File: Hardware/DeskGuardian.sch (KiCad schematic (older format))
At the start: 7 parts

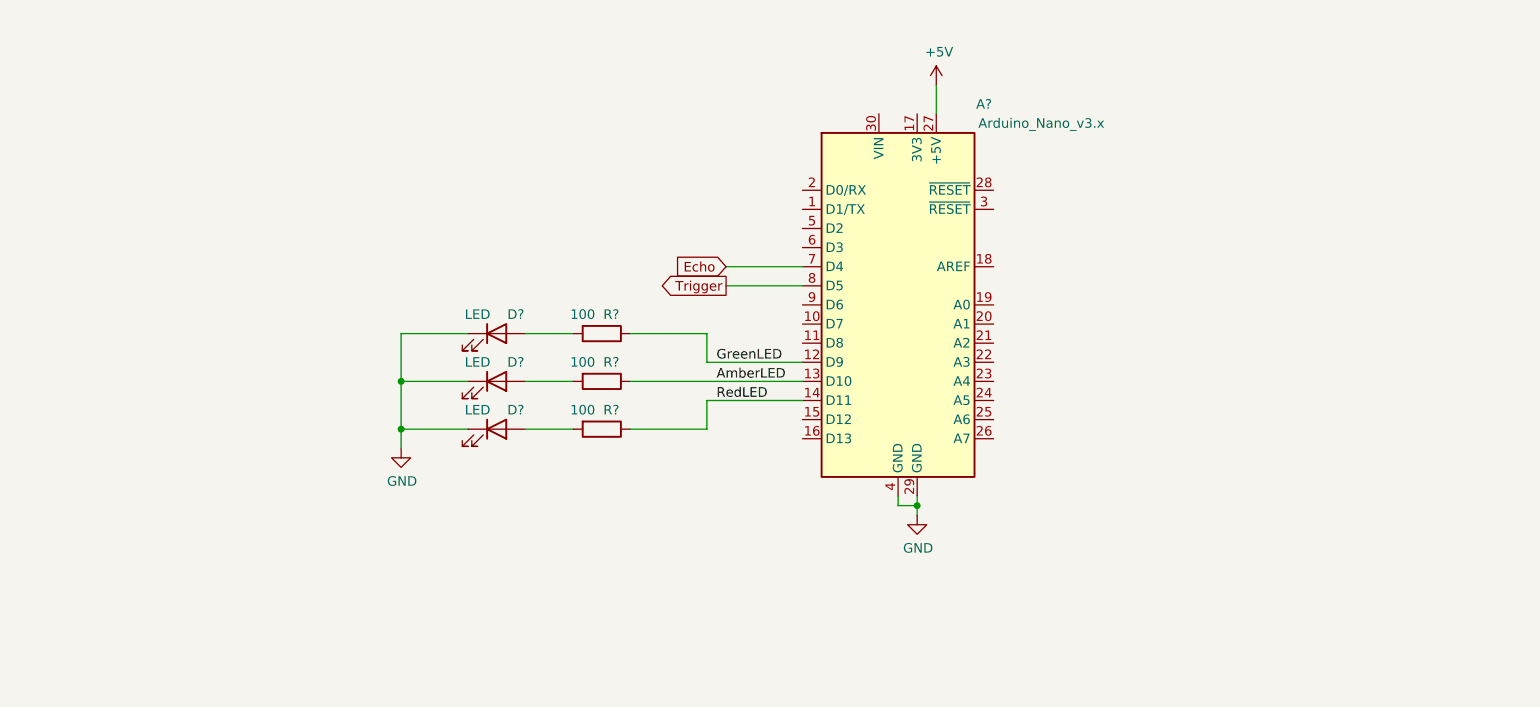
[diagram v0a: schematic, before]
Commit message: Full rework of instructions
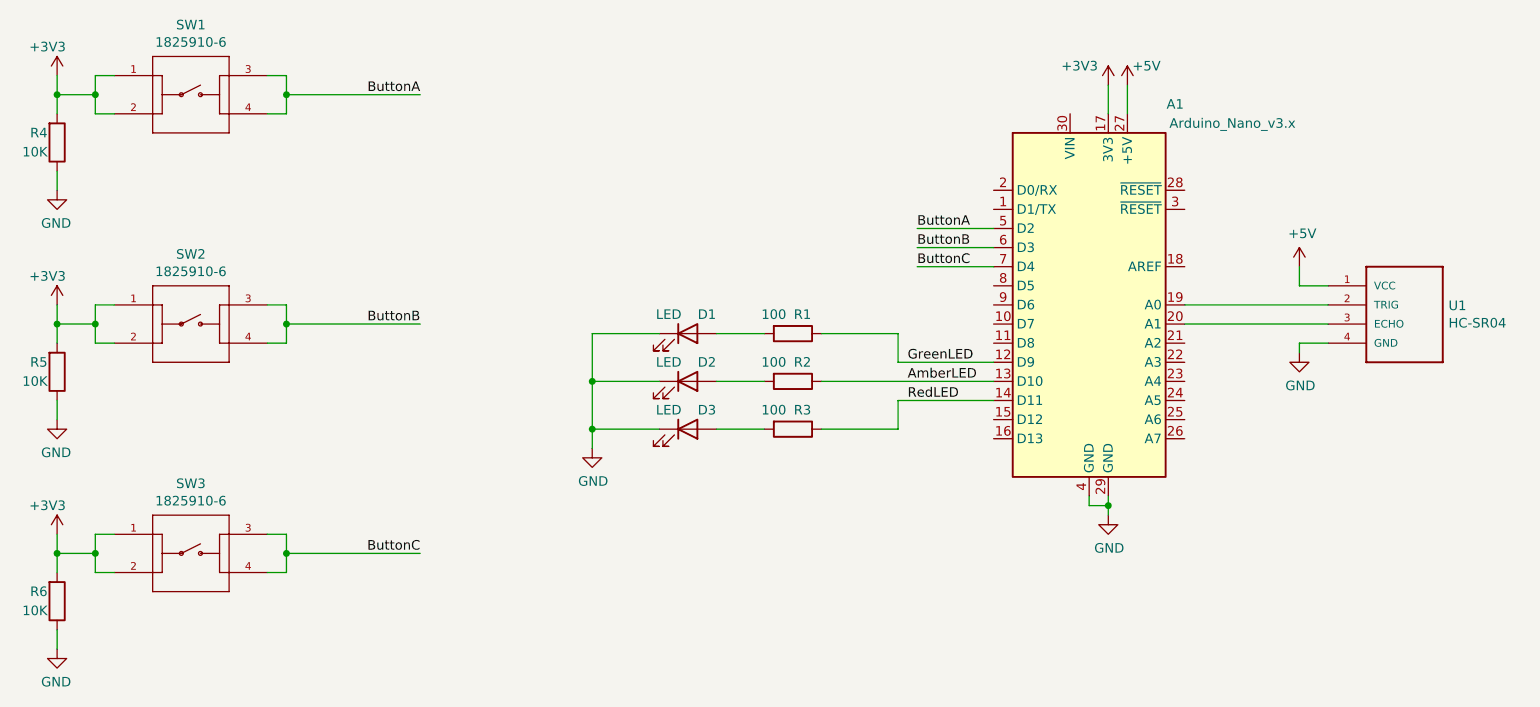
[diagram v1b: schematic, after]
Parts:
- added R4, R5, R6: 10K, symbol Device:R
- added SW1, SW2, SW3: 1825910-6, SW_1825910-6-4, symbol 1825910-6:1825910-6
- added U1: HC-SR04, XCVR_HC-SR04, symbol HC-SR04:HC-SR04
- gave numbers to parts that had none: 7
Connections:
- net +5V: now also U1.1 (VCC)
- net GND: now also R4.1, R5.1, R6.1, U1.4 (GND)
- net +3V3: now reaches A1.17 (3V3)
- net +3V3: now also R4.2, R5.2, R6.2, SW1.1, SW1.2, SW2.1, SW2.2, SW3.1, SW3.2
- net at A1.19 (A0): now also U1.2 (TRIG)
- net at A1.20 (A1): now also U1.3 (ECHO)
- net ButtonA: now reaches A1.5 (D2)
- net ButtonA: now also SW1.3, SW1.4
- net ButtonB: now reaches A1.6 (D3)
- net ButtonB: now also SW2.3, SW2.4
- net Echo renamed ButtonC
- net ButtonC: now also SW3.3, SW3.4
- net Trigger: no longer names the net of A1.8 (D5)
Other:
- moved on the sheet: A1, D1, D2, D3, R1, R2, R3

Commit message: updated schematic
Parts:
- D1, D2, D3: footprint (none) -> LED_THT:LED_D5.0mm
- R1: renamed from R4; footprint (none) -> Resistor_SMD:R_1206_3216Metric_Pad1.42x1.75mm_HandSolder
- R2: renamed from R5; footprint (none) -> Resistor_SMD:R_1206_3216Metric_Pad1.42x1.75mm_HandSolder
- R3: renamed from R6; footprint (none) -> Resistor_SMD:R_1206_3216Metric_Pad1.42x1.75mm_HandSolder
- R4: renamed from R1; footprint (none) -> Resistor_SMD:R_1206_3216Metric_Pad1.42x1.75mm_HandSolder
- R5: renamed from R2; footprint (none) -> Resistor_SMD:R_1206_3216Metric_Pad1.42x1.75mm_HandSolder
- R6: renamed from R3; footprint (none) -> Resistor_SMD:R_1206_3216Metric_Pad1.42x1.75mm_HandSolder
- SW1, SW2, SW3: footprint SW_1825910-6-4 -> Footprints:SW_1825910-6-4
- U1: footprint XCVR_HC-SR04 -> Footprints:XCVR_HC-SR04
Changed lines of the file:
@@
 $EndDescr
 $Comp
-L power:GND #PWR0101
+L power:GND #PWR09
 U 1 1 5F31EFDB
 P 7000 4500
-F 0 "#PWR0101" H 7000 4250 50  0001 C CNN
+F 0 "#PWR09" H 7000 4250 50  0001 C CNN
 F 1 "GND" H 7005 4327 50  0000 C CNN
 F 2 "" H 7000 4500 50  0001 C CNN
@@
 $EndComp
 $Comp
-L Device:R R4
+L Device:R R1
 U 1 1 5F35D6A2
 P 1500 2550
-F 0 "R4" H 1450 2500 50  0000 R CNN
+F 0 "R1" H 1450 2500 50  0000 R CNN
 F 1 "10K" H 1450 2600 50  0000 R CNN
-F 2 "" V 1430 2550 50  0001 C CNN
+F 2 "Resistor_SMD:R_1206_3216Metric_Pad1.42x1.75mm_HandSolder" V 1430 2550 50  0001 C CNN
 F 3 "~" H 1500 2550 50  0001 C CNN
 	1    1500 2550
@@
 	7000 2400 7000 2250
 $Comp
-L power:+5V #PWR0102
+L power:+5V #PWR010
 U 1 1 5F31F7F8
 P 7100 2250
-F 0 "#PWR0102" H 7100 2100 50  0001 C CNN
+F 0 "#PWR010" H 7100 2100 50  0001 C CNN
 F 1 "+5V" H 7200 2350 50  0000 C CNN
 F 2 "" H 7100 2250 50  0001 C CNN
@@
 $EndComp
 $Comp
-L power:+3V3 #PWR05
+L power:+3V3 #PWR08
 U 1 1 5F39EB8C
 P 7000 2250
-F 0 "#PWR05" H 7000 2100 50  0001 C CNN
+F 0 "#PWR08" H 7000 2100 50  0001 C CNN
 F 1 "+3V3" H 6850 2350 50  0000 C CNN
 F 2 "" H 7000 2250 50  0001 C CNN
@@
 	8150 3300 8000 3300
 $Comp
-L power:+5V #PWR06
+L power:+5V #PWR011
 U 1 1 5F3582F6
 P 8000 3200
-F 0 "#PWR06" H 8000 3050 50  0001 C CNN
+F 0 "#PWR011" H 8000 3050 50  0001 C CNN
 F 1 "+5V" H 8015 3373 50  0000 C CNN
 F 2 "" H 8000 3200 50  0001 C CNN
@@
 $EndComp
 $Comp
-L power:GND #PWR07
+L power:GND #PWR012
 U 1 1 5F357FB1
 P 8000 3650
-F 0 "#PWR07" H 8000 3400 50  0001 C CNN
+F 0 "#PWR012" H 8000 3400 50  0001 C CNN
 F 1 "GND" H 8005 3477 50  0000 C CNN
 F 2 "" H 8000 3650 50  0001 C CNN
@@
 F 0 "U1" H 8780 3396 50  0000 L CNN
 F 1 "HC-SR04" H 8780 3305 50  0000 L CNN
-F 2 "XCVR_HC-SR04" H 8350 3400 50  0001 L BNN
+F 2 "Footprints:XCVR_HC-SR04" H 8350 3400 50  0001 L BNN
 F 3 "Osepp" H 8350 3400 50  0001 L BNN
 	1    8350 3400
@@
 	6400 3000 6000 3000
 $Comp
-L Device:R R1
+L Device:R R4
 U 1 1 5F338E4B
 P 5350 3550
-F 0 "R1" V 5250 3600 50  0000 C CNN
+F 0 "R4" V 5250 3600 50  0000 C CNN
 F 1 "100" V 5250 3450 50  0000 C CNN
-F 2 "" V 5280 3550 50  0001 C CNN
+F 2 "Resistor_SMD:R_1206_3216Metric_Pad1.42x1.75mm_HandSolder" V 5280 3550 50  0001 C CNN
 F 3 "~" H 5350 3550 50  0001 C CNN
 	1    5350 3550
@@
 $EndComp
 $Comp
-L Device:R R2
+L Device:R R5
 U 1 1 5F3392D8
 P 5350 3800
-F 0 "R2" V 5250 3850 50  0000 C CNN
+F 0 "R5" V 5250 3850 50  0000 C CNN
 F 1 "100" V 5250 3700 50  0000 C CNN
-F 2 "" V 5280 3800 50  0001 C CNN
+F 2 "Resistor_SMD:R_1206_3216Metric_Pad1.42x1.75mm_HandSolder" V 5280 3800 50  0001 C CNN
 F 3 "~" H 5350 3800 50  0001 C CNN
 	1    5350 3800
@@
 	4650 4050 4300 4050
 $Comp
-L power:GND #PWR0103
+L power:GND #PWR07
 U 1 1 5F33E95F
 P 4300 4150
-F 0 "#PWR0103" H 4300 3900 50  0001 C CNN
+F 0 "#PWR07" H 4300 3900 50  0001 C CNN
 F 1 "GND" H 4305 3977 50  0000 C CNN
 F 2 "" H 4300 4150 50  0001 C CNN
@@
 	5200 3800 4950 3800
 $Comp
-L Device:R R3
+L Device:R R6
 U 1 1 5F3395DB
 P 5350 4050
-F 0 "R3" V 5250 4100 50  0000 C CNN
+F 0 "R6" V 5250 4100 50  0000 C CNN
 F 1 "100" V 5250 3950 50  0000 C CNN
-F 2 "" V 5280 4050 50  0001 C CNN
+F 2 "Resistor_SMD:R_1206_3216Metric_Pad1.42x1.75mm_HandSolder" V 5280 4050 50  0001 C CNN
 F 3 "~" H 5350 4050 50  0001 C CNN
 	1    5350 4050
@@
 F 0 "D3" H 4900 4150 50  0000 C CNN
 F 1 "LED" H 4700 4150 50  0000 C CNN
-F 2 "" H 4800 4050 50  0001 C CNN
+F 2 "LED_THT:LED_D5.0mm" H 4800 4050 50  0001 C CNN
 F 3 "~" H 4800 4050 50  0001 C CNN
 	1    4800 4050
@@
 F 0 "D2" H 4900 3900 50  0000 C CNN
 F 1 "LED" H 4700 3900 50  0000 C CNN
-F 2 "" H 4800 3800 50  0001 C CNN
+F 2 "LED_THT:LED_D5.0mm" H 4800 3800 50  0001 C CNN
 F 3 "~" H 4800 3800 50  0001 C CNN
 	1    4800 3800
@@
 F 0 "D1" H 4900 3650 50  0000 C CNN
 F 1 "LED" H 4700 3650 50  0000 C CNN
-F 2 "" H 4800 3550 50  0001 C CNN
+F 2 "LED_THT:LED_D5.0mm" H 4800 3550 50  0001 C CNN
 F 3 "~" H 4800 3550 50  0001 C CNN
 	1    4800 3550
@@
 F 0 "SW1" H 2200 2665 50  0000 C CNN
 F 1 "1825910-6" H 2200 2574 50  0000 C CNN
-F 2 "SW_1825910-6-4" H 2200 2300 50  0001 L BNN
+F 2 "Footprints:SW_1825910-6-4" H 2200 2300 50  0001 L BNN
 F 3 "Compliant" H 2200 2300 50  0001 L BNN
 F 4 "50 mA" H 2200 2300 50  0001 L BNN "Field4"
@@
 Connection ~ 2700 2300
 $Comp
-L Device:R R5
+L Device:R R2
 U 1 1 5F40E2B9
 P 1500 3750
-F 0 "R5" H 1450 3700 50  0000 R CNN
+F 0 "R2" H 1450 3700 50  0000 R CNN
 F 1 "10K" H 1450 3800 50  0000 R CNN
-F 2 "" V 1430 3750 50  0001 C CNN
+F 2 "Resistor_SMD:R_1206_3216Metric_Pad1.42x1.75mm_HandSolder" V 1430 3750 50  0001 C CNN
 F 3 "~" H 1500 3750 50  0001 C CNN
 	1    1500 3750
@@
 F 0 "SW2" H 2200 3865 50  0000 C CNN
 F 1 "1825910-6" H 2200 3774 50  0000 C CNN
-F 2 "SW_1825910-6-4" H 2200 3500 50  0001 L BNN
+F 2 "Footprints:SW_1825910-6-4" H 2200 3500 50  0001 L BNN
 F 3 "Compliant" H 2200 3500 50  0001 L BNN
 F 4 "50 mA" H 2200 3500 50  0001 L BNN "Field4"
@@
 Connection ~ 2700 3500
 $Comp
-L Device:R R6
+L Device:R R3
 U 1 1 5F41D33F
 P 1500 4950
-F 0 "R6" H 1450 4900 50  0000 R CNN
+F 0 "R3" H 1450 4900 50  0000 R CNN
 F 1 "10K" H 1450 5000 50  0000 R CNN
-F 2 "" V 1430 4950 50  0001 C CNN
+F 2 "Resistor_SMD:R_1206_3216Metric_Pad1.42x1.75mm_HandSolder" V 1430 4950 50  0001 C CNN
 F 3 "~" H 1500 4950 50  0001 C CNN
 	1    1500 4950
@@
 $EndComp
 $Comp
-L power:GND #PWR09
+L power:GND #PWR06
 U 1 1 5F41D345
 P 1500 5200
-F 0 "#PWR09" H 1500 4950 50  0001 C CNN
+F 0 "#PWR06" H 1500 4950 50  0001 C CNN
 F 1 "GND" H 1505 5027 50  0000 C CNN
 F 2 "" H 1500 5200 50  0001 C CNN
@@
 ButtonC
 $Comp
-L power:+3V3 #PWR08
+L power:+3V3 #PWR05
 U 1 1 5F41D351
 P 1500 4600
-F 0 "#PWR08" H 1500 4450 50  0001 C CNN
+F 0 "#PWR05" H 1500 4450 50  0001 C CNN
 F 1 "+3V3" H 1450 4750 50  0000 C CNN
 F 2 "" H 1500 4600 50  0001 C CNN
@@
 F 0 "SW3" H 2200 5065 50  0000 C CNN
 F 1 "1825910-6" H 2200 4974 50  0000 C CNN
-F 2 "SW_1825910-6-4" H 2200 4700 50  0001 L BNN
+F 2 "Footprints:SW_1825910-6-4" H 2200 4700 50  0001 L BNN
 F 3 "Compliant" H 2200 4700 50  0001 L BNN
 F 4 "50 mA" H 2200 4700 50  0001 L BNN "Field4"
